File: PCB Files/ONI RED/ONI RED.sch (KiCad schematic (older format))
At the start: 1 part

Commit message: Continued work on power supplies and added new ICs to design
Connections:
- net labels added: +3.3V
- wire segments 0 -> 5
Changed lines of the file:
@@
 EELAYER 30 0
 EELAYER END
-$Descr A4 11693 8268
+$Descr A3 16535 11693
 encoding utf-8
-Sheet 1 1
+Sheet 1 4
 Title ""
 Date ""
@@
 L Custom~Symbols:PCI-Express-4x U?
 U 1 1 5E9718C0
-P 5750 3450
-F 0 "U?" H 5775 5115 50  0000 C CNN
-F 1 "PCI-Express-4x" H 5775 5024 50  0000 C CNN
-F 2 "" H 4750 5000 50  0001 C CNN
-F 3 "" H 4750 5000 50  0001 C CNN
-	1    5750 3450
+P 9800 4700
+F 0 "U?" H 9825 6365 50  0000 C CNN
+F 1 "PCI-Express-4x" H 9825 6274 50  0000 C CNN
+F 2 "" H 8800 6250 50  0001 C CNN
+F 3 "" H 8800 6250 50  0001 C CNN
+	1    9800 4700
 	1    0    0    -1
 $EndComp
+$Sheet
+S 1800 5100 1450 1150
+U 5EA74211
+F0 "Sheet5EA74210" 50
+F1 "PHY.sch" 50
+F2 "+3.3V" I R 3250 5650 50
+F3 "GND" I R 3250 5800 50
+$EndSheet
+$Sheet
+S 1800 3250 1450 1250
+U 5E980F81
+F0 "Sheet5E980F80" 50
+F1 "PSU.sch" 50
+F2 "+3.3V" I R 3250 4350 50
+F3 "GND" B R 3250 4250 50
+F4 "+1.1V_(VCC)" O R 3250 4150 50
+F5 "+2.5V_(VCC_AUX)" O R 3250 4050 50
+$EndSheet
+$Sheet
+S 1800 6800 1450 1200
+U 5EAC1072
+F0 "Sheet5EAC1071" 50
+F1 "FPGA Main.sch" 50
+F2 "+3.3V" I R 3250 7000 50
+F3 "GND" I R 3250 7100 50
+$EndSheet
+Wire Wire Line
+	9000 4200 8600 4200
+Wire Wire Line
+	8600 4200 8600 4150
+Wire Wire Line
+	8600 4100 9000 4100
+Text GLabel 8350 4150 0    50   Output ~ 0
++3.3V
+Wire Wire Line
+	8350 4150 8600 4150
+Connection ~ 8600 4150
+Wire Wire Line
+	8600 4150 8600 4100
 $EndSCHEMATC

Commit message: Added second ethernet PHY and started to add PCIE connections
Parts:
- U?: symbol Custom~Symbols:PCI-Express-4x -> Custom_Symbols:PCI-Express-4X
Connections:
- net labels added: +12V, GND, HSI(0), HSI(1), HSO(0), HSO(1), PRST, REFCLK
- wire segments 5 -> 80
- no-connect marks 0 -> 12

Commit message: Continued routing work
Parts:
- added C1, C6: 0.1uF, symbol Device:CP1_Small
- added C2, C5: 22uF, symbol Device:CP1_Small
- added C3, C4: 0.01uF, symbol Device:CP1_Small
- added U10: LFE5UM-25F-6BG381C, symbol Custom_Symbols:LFE5UM-25F-6BG381C
- gave numbers to parts that had none: 1
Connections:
- net Sheet5E980F80/+1.1V_(VCC): now also C1.1, C2.1, C3.1, C4.1, C5.1, C6.1, U10.H10 (VCC), U10.H11 (VCC), U10.H12 (VCC), U10.H13 (VCC), U10.H8 (VCC), U10.H9 (VCC), U10.J13 (VCC), U10.K13 (VCC), U10.K8 (VCC), U10.L13 (VCC), U10.M13 (VCC), U10.M8 (VCC), U10.N10 (VCC), U10.N11 (VCC), U10.N12 (VCC), U10.N13 (VCC), U10.N8 (VCC), U10.N9 (VCC), U10.T10 (VCCHTX1), U10.T7 (VCCHTX0), U10.T8 (VCCHRX0), U10.T9 (VCCHRX1)
- net Sheet5E980F80/+1.1V_(VCCA): now also U10.T6 (VCCA0), U10.U6 (VCCA0)
- net Sheet5E980F80/+2.5V_(VCC_AUX): now also U10.F15 (VCCAUX), U10.F6 (VCCAUX), U10.P15 (VCCAUX), U10.P6 (VCCAUX), U10.V10 (VCCAUXA0), U10.V11 (VCCAUXA0)
- net Sheet5E980F80/GND: now also C1.2, C4.2, C5.2, U10.B14 (GND), U10.B7 (GND), U10.C19 (GND), U10.D4 (GND), U10.F13 (GND), U10.F14 (GND), U10.F7 (GND), U10.F8 (GND), U10.G10 (GND), U10.G11 (GND), U10.G12 (GND), U10.G13 (GND), U10.G14 (GND), U10.G15 (GND), U10.G17 (GND), U10.G4 (GND), U10.G6 (GND), U10.G7 (GND), U10.G8 (GND), U10.G9 (GND), U10.H19 (GND), U10.J10 (GND), U10.J11 (GND), U10.J12 (GND), U10.J14 (GND), U10.J2 (GND), U10.J7 (GND), U10.J9 (GND), U10.K10 (GND), U10.K11 (GND), U10.K12 (GND), U10.K14 (GND), U10.K15 (GND), U10.K6 (GND), U10.K7 (GND), U10.K9 (GND), U10.L10 (GND), U10.L11 (GND), U10.L12 (GND), U10.L9 (GND), U10.M10 (GND), U10.M11 (GND), U10.M12 (GND), U10.M14 (GND), U10.M16 (GND), U10.M2 (GND), U10.M7 (GND), U10.M9 (GND), U10.N14 (GND), U10.N15 (GND), U10.N6 (GND), U10.N7 (GND), U10.P11 (GND), U10.P12 (GND), U10.P13 (GND), U10.P14 (GND), U10.P7 (GND), U10.P8 (GND), U10.R19 (GND), U10.U10 (GND), U10.U11 (GND), U10.U12 (GND), U10.U13 (GND), U10.U14 (GND), U10.U7 (GND), U10.U8 (GND), U10.U9 (GND), U10.V12 (GND), U10.V13 (GND), U10.V14 (GND), U10.V15 (GND), U10.V16 (GND), U10.V19 (GND), U10.V20 (GND), U10.V5 (GND), U10.V6 (GND), U10.V7 (GND), U10.V8 (GND), U10.V9 (GND), U10.W12 (GND), U10.W15 (GND), U10.W16 (GND), U10.W19 (GND), U10.W6 (GND), U10.W7 (GND)
- net CLKP: now reaches U2.13A (REFCLK+)
- net CLKN: now reaches U2.14A (REFCLK-)
- net RXP0: now reaches U2.14B (HSOp(0))
- net RXN0: now reaches U2.15B (HSOn(0))
- net TXP0: now reaches U2.16A (HSIp(0))
- net TXN0: now reaches U2.17A (HSIn(0))
- net RXP1: now reaches U2.19B (HSOp(1))
- net RXN1: now reaches U2.20B (HSOn(1))
- net TXP1: now reaches U2.21A (HSIp(1))
- net TXN1: now reaches U2.22A (HSIn(1))
- new net: C2.2, C3.2, C6.2
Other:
- note added: "VCCH Filter\n"

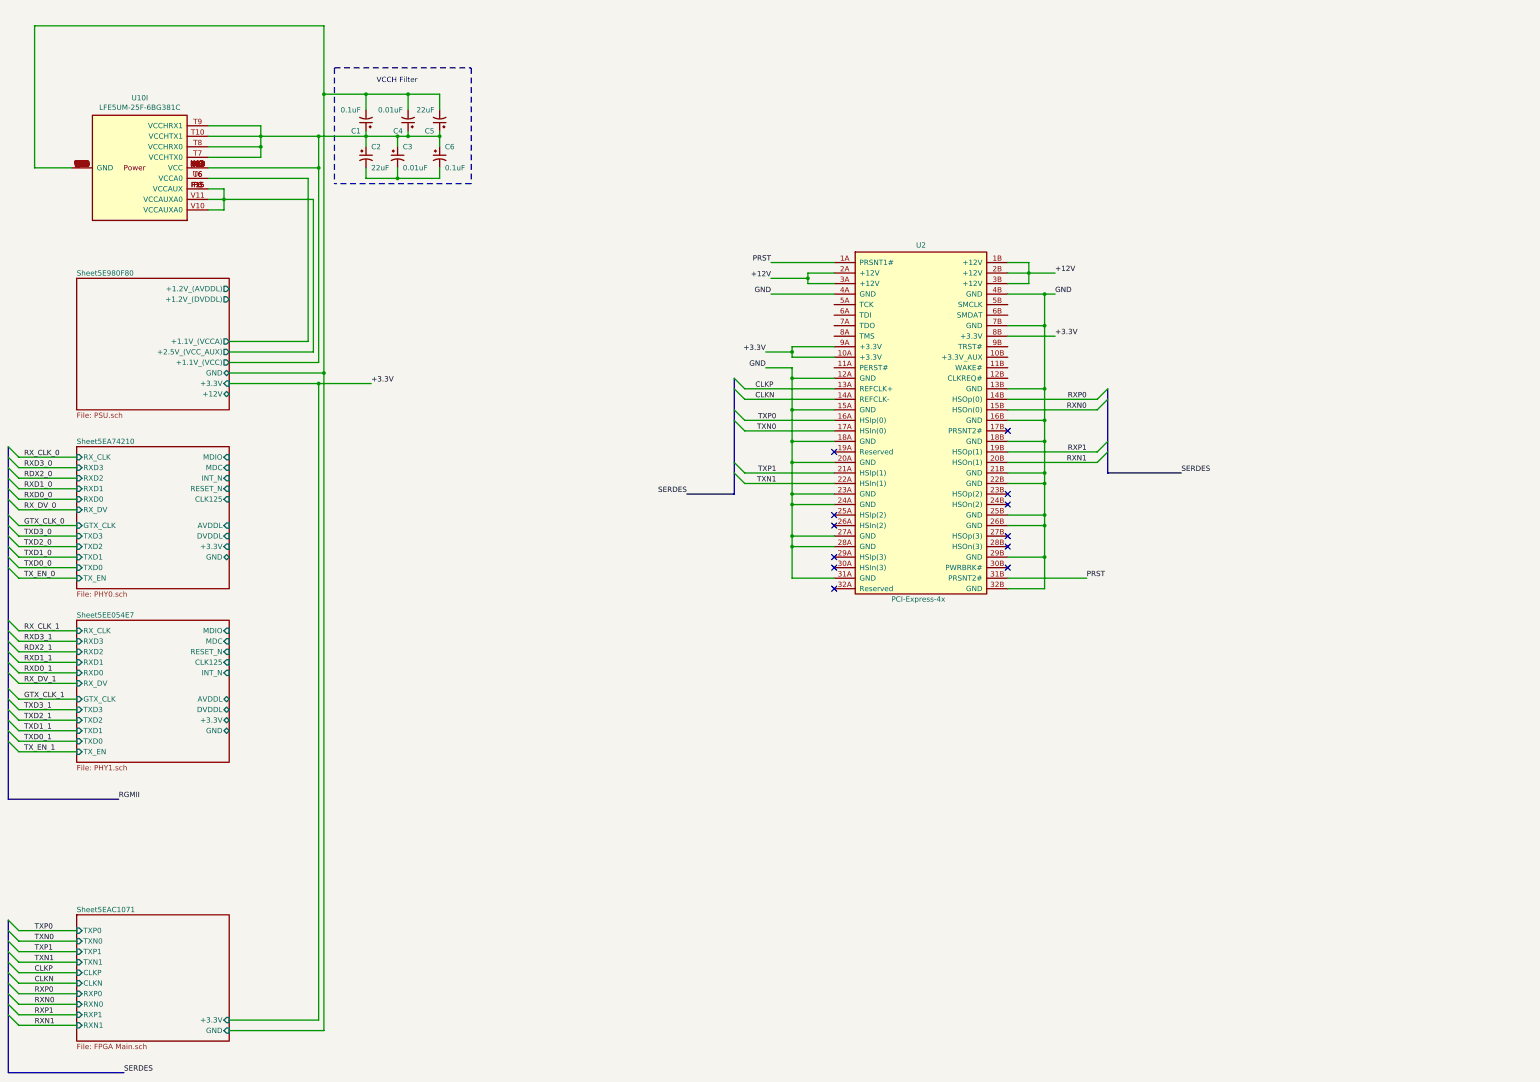
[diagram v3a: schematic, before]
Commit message: Began routing PHY IO
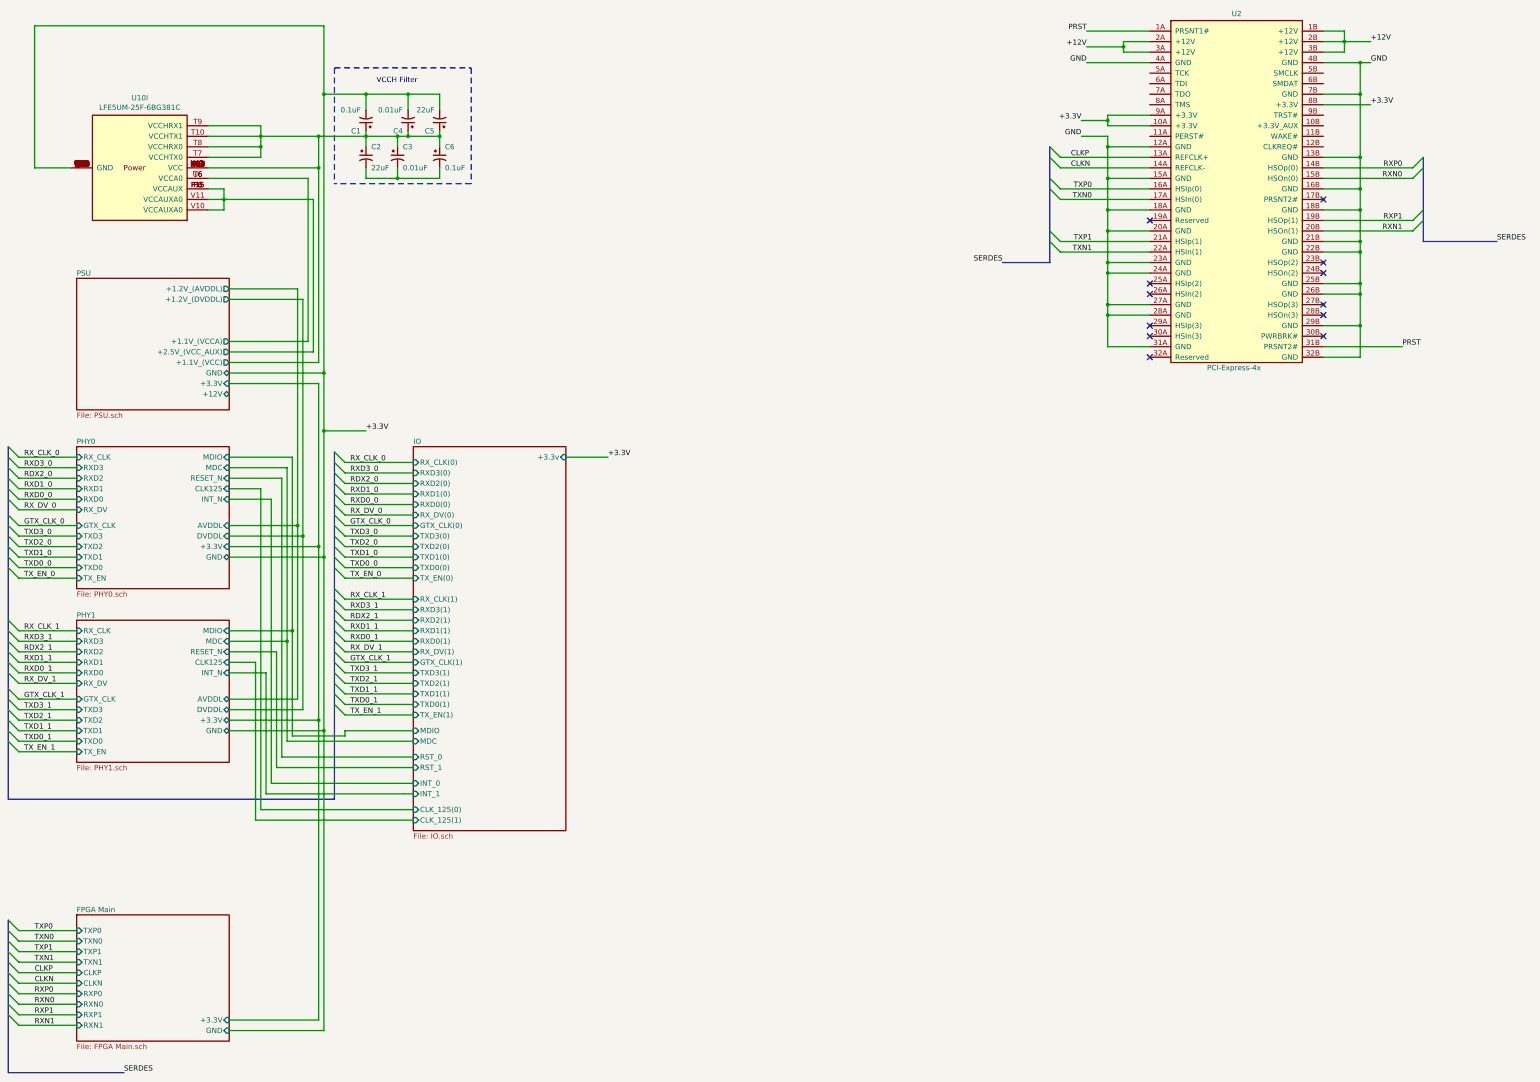
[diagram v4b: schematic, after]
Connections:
- net Sheet5E980F80/GND is gone; now on net +3.3V: C1.2, C4.2, C5.2, U10.B14 (GND), U10.B7 (GND), U10.C19 (GND), U10.D4 (GND), U10.F13 (GND), U10.F14 (GND), U10.F7 (GND), U10.F8 (GND), U10.G10 (GND), U10.G11 (GND), U10.G12 (GND), U10.G13 (GND), U10.G14 (GND), U10.G15 (GND), U10.G17 (GND), U10.G4 (GND), U10.G6 (GND), U10.G7 (GND), U10.G8 (GND), U10.G9 (GND), U10.H19 (GND), U10.J10 (GND), U10.J11 (GND), U10.J12 (GND), U10.J14 (GND), U10.J2 (GND), U10.J7 (GND), U10.J9 (GND), U10.K10 (GND), U10.K11 (GND), U10.K12 (GND), U10.K14 (GND), U10.K15 (GND), U10.K6 (GND), U10.K7 (GND), U10.K9 (GND), U10.L10 (GND), U10.L11 (GND), U10.L12 (GND), U10.L9 (GND), U10.M10 (GND), U10.M11 (GND), U10.M12 (GND), U10.M14 (GND), U10.M16 (GND), U10.M2 (GND), U10.M7 (GND), U10.M9 (GND), U10.N14 (GND), U10.N15 (GND), U10.N6 (GND), U10.N7 (GND), U10.P11 (GND), U10.P12 (GND), U10.P13 (GND), U10.P14 (GND), U10.P7 (GND), U10.P8 (GND), U10.R19 (GND), U10.U10 (GND), U10.U11 (GND), U10.U12 (GND), U10.U13 (GND), U10.U14 (GND), U10.U7 (GND), U10.U8 (GND), U10.U9 (GND), U10.V12 (GND), U10.V13 (GND), U10.V14 (GND), U10.V15 (GND), U10.V16 (GND), U10.V19 (GND), U10.V20 (GND), U10.V5 (GND), U10.V6 (GND), U10.V7 (GND), U10.V8 (GND), U10.V9 (GND), U10.W12 (GND), U10.W15 (GND), U10.W16 (GND), U10.W19 (GND), U10.W6 (GND), U10.W7 (GND)
- net Sheet5E980F80/+1.1V_(VCC) renamed PSU/+1.1V_(VCC)
- net Sheet5E980F80/+1.1V_(VCCA) renamed PSU/+1.1V_(VCCA)
- net Sheet5E980F80/+2.5V_(VCC_AUX) renamed PSU/+2.5V_(VCC_AUX)
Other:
- moved on the sheet: U2

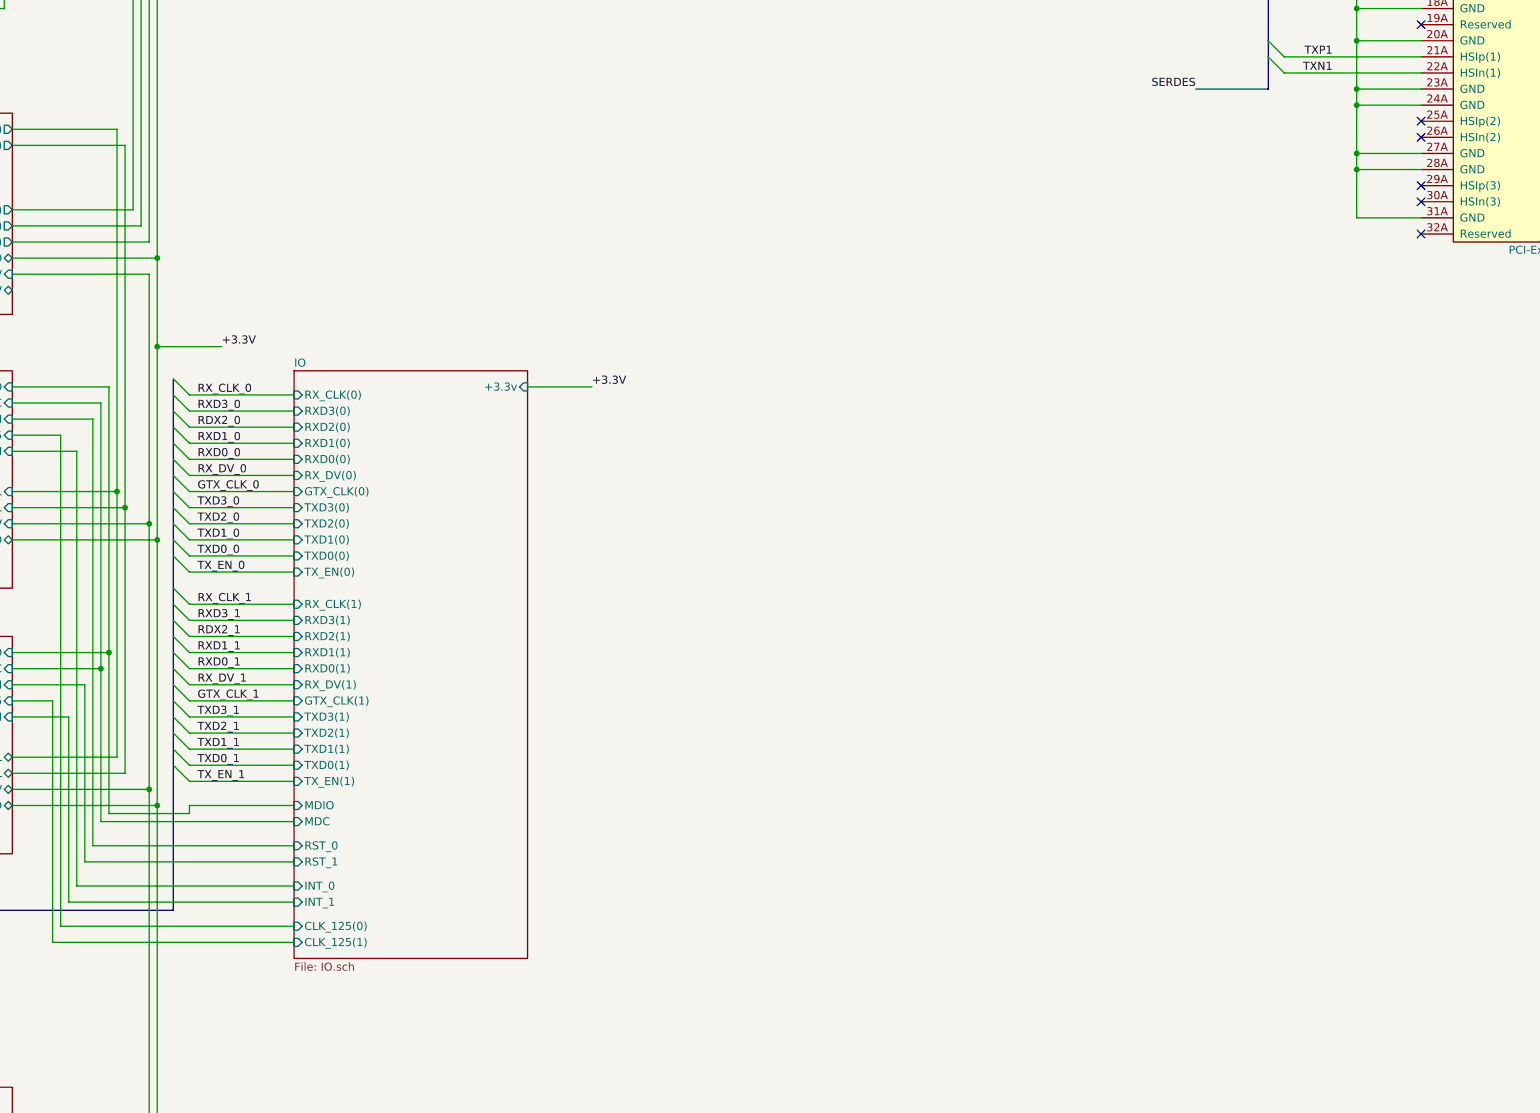
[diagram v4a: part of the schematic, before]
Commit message: Added extra PHYs and expanded IO
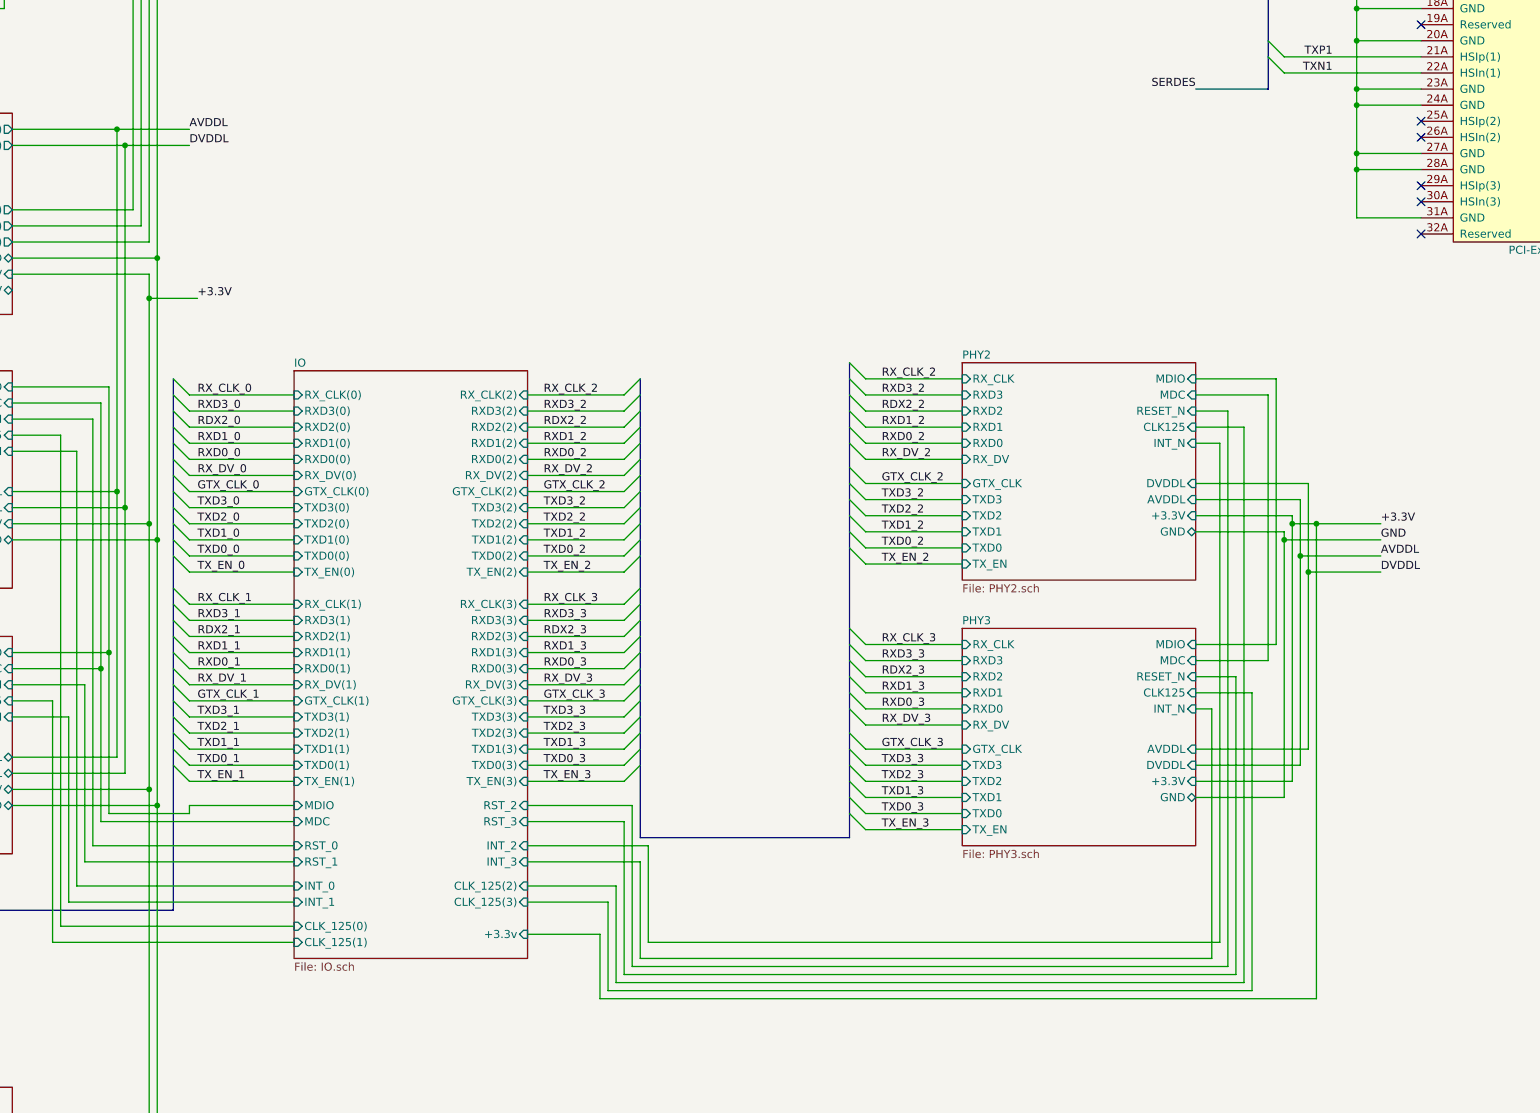
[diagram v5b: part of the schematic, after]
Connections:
- net +3.3V: no longer C1.2, C4.2, C5.2, U10.B14 (GND), U10.B7 (GND), U10.C19 (GND), U10.D4 (GND), U10.F13 (GND), U10.F14 (GND), U10.F7 (GND), U10.F8 (GND), U10.G10 (GND), U10.G11 (GND), U10.G12 (GND), U10.G13 (GND), U10.G14 (GND), U10.G15 (GND), U10.G17 (GND), U10.G4 (GND), U10.G6 (GND), U10.G7 (GND), U10.G8 (GND), U10.G9 (GND), U10.H19 (GND), U10.J10 (GND), U10.J11 (GND), U10.J12 (GND), U10.J14 (GND), U10.J2 (GND), U10.J7 (GND), U10.J9 (GND), U10.K10 (GND), U10.K11 (GND), U10.K12 (GND), U10.K14 (GND), U10.K15 (GND), U10.K6 (GND), U10.K7 (GND), U10.K9 (GND), U10.L10 (GND), U10.L11 (GND), U10.L12 (GND), U10.L9 (GND), U10.M10 (GND), U10.M11 (GND), U10.M12 (GND), U10.M14 (GND), U10.M16 (GND), U10.M2 (GND), U10.M7 (GND), U10.M9 (GND), U10.N14 (GND), U10.N15 (GND), U10.N6 (GND), U10.N7 (GND), U10.P11 (GND), U10.P12 (GND), U10.P13 (GND), U10.P14 (GND), U10.P7 (GND), U10.P8 (GND), U10.R19 (GND), U10.U10 (GND), U10.U11 (GND), U10.U12 (GND), U10.U13 (GND), U10.U14 (GND), U10.U7 (GND), U10.U8 (GND), U10.U9 (GND), U10.V12 (GND), U10.V13 (GND), U10.V14 (GND), U10.V15 (GND), U10.V16 (GND), U10.V19 (GND), U10.V20 (GND), U10.V5 (GND), U10.V6 (GND), U10.V7 (GND), U10.V8 (GND), U10.V9 (GND), U10.W12 (GND), U10.W15 (GND), U10.W16 (GND), U10.W19 (GND), U10.W6 (GND), U10.W7 (GND)
- new net FPGA Main/GND: C1.2, C4.2, C5.2, U10.B14 (GND), U10.B7 (GND), U10.C19 (GND), U10.D4 (GND), U10.F13 (GND), U10.F14 (GND), U10.F7 (GND), U10.F8 (GND), U10.G10 (GND), U10.G11 (GND), U10.G12 (GND), U10.G13 (GND), U10.G14 (GND), U10.G15 (GND), U10.G17 (GND), U10.G4 (GND), U10.G6 (GND), U10.G7 (GND), U10.G8 (GND), U10.G9 (GND), U10.H19 (GND), U10.J10 (GND), U10.J11 (GND), U10.J12 (GND), U10.J14 (GND), U10.J2 (GND), U10.J7 (GND), U10.J9 (GND), U10.K10 (GND), U10.K11 (GND), U10.K12 (GND), U10.K14 (GND), U10.K15 (GND), U10.K6 (GND), U10.K7 (GND), U10.K9 (GND), U10.L10 (GND), U10.L11 (GND), U10.L12 (GND), U10.L9 (GND), U10.M10 (GND), U10.M11 (GND), U10.M12 (GND), U10.M14 (GND), U10.M16 (GND), U10.M2 (GND), U10.M7 (GND), U10.M9 (GND), U10.N14 (GND), U10.N15 (GND), U10.N6 (GND), U10.N7 (GND), U10.P11 (GND), U10.P12 (GND), U10.P13 (GND), U10.P14 (GND), U10.P7 (GND), U10.P8 (GND), U10.R19 (GND), U10.U10 (GND), U10.U11 (GND), U10.U12 (GND), U10.U13 (GND), U10.U14 (GND), U10.U7 (GND), U10.U8 (GND), U10.U9 (GND), U10.V12 (GND), U10.V13 (GND), U10.V14 (GND), U10.V15 (GND), U10.V16 (GND), U10.V19 (GND), U10.V20 (GND), U10.V5 (GND), U10.V6 (GND), U10.V7 (GND), U10.V8 (GND), U10.V9 (GND), U10.W12 (GND), U10.W15 (GND), U10.W16 (GND), U10.W19 (GND), U10.W6 (GND), U10.W7 (GND)
